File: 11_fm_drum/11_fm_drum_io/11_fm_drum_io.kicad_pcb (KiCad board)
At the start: 2 copper layers, 11 parts, among them J1 Conn_02x10_Counter_Clockwise, SW1 SW_SPDT, SW2 SW_SPDT

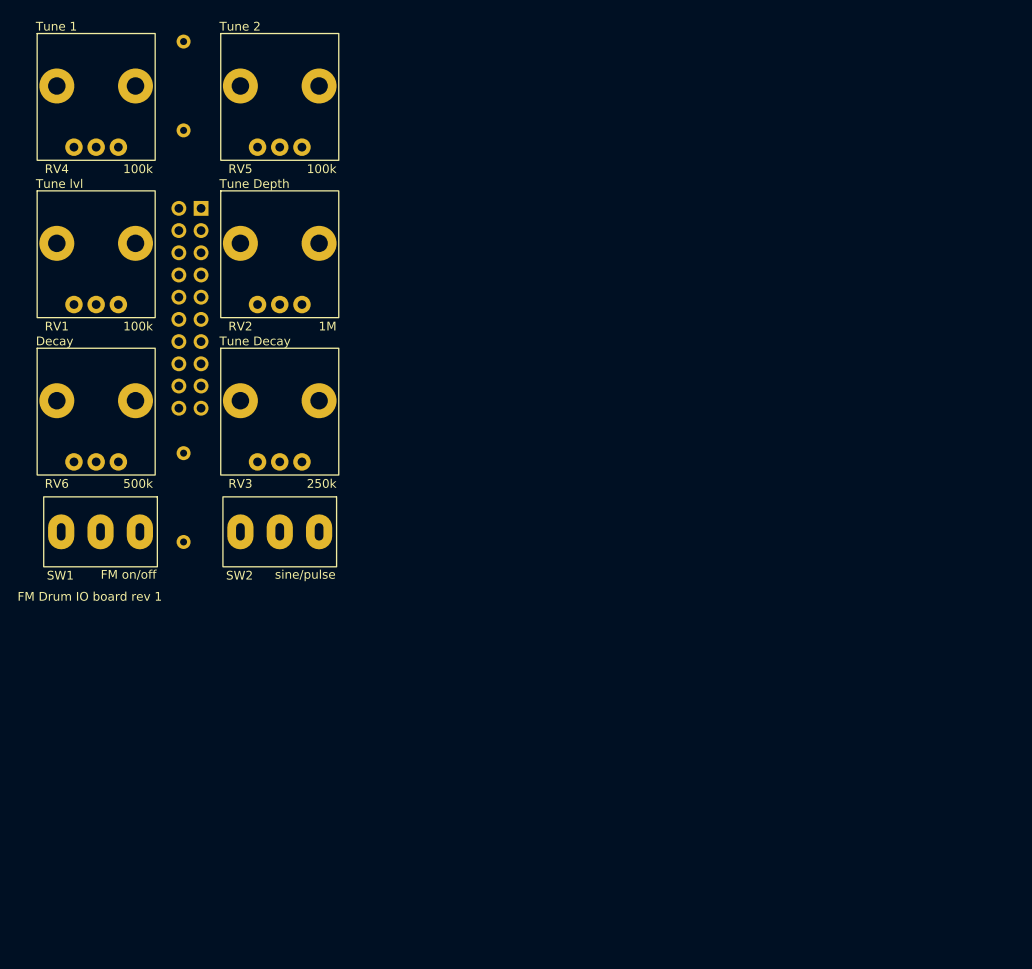
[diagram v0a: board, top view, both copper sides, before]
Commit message: removed io from 11
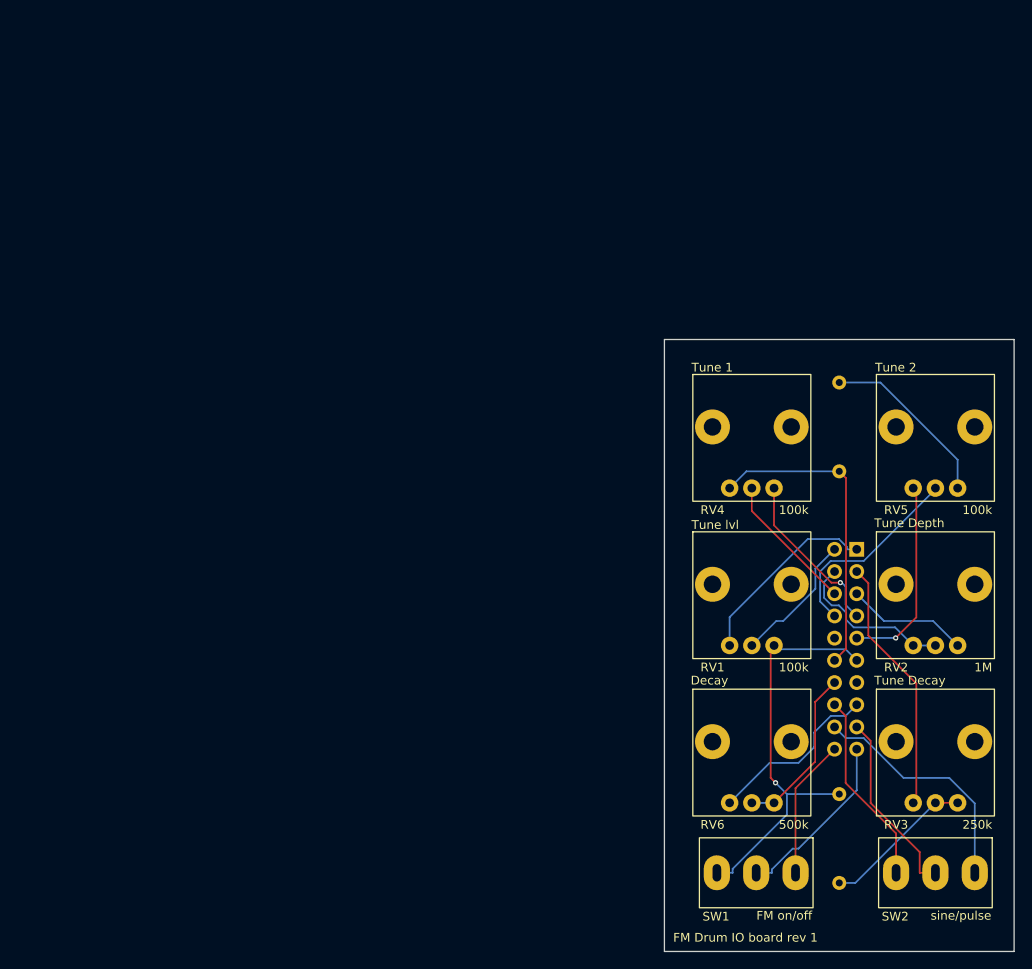
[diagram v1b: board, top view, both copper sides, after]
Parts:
- moved J1 84.5 mm to (97.0, 63.0)
- moved R1 84.5 mm to (95.0, 43.9)
- moved R2 84.5 mm to (95.0, 91.0)
- moved RV1 84.5 mm to (85.0, 67.0)
- moved RV2 84.5 mm to (106.0, 67.0)
- moved RV3 84.5 mm to (106.0, 85.0)
- moved RV4 84.5 mm to (85.0, 49.0)
- moved RV5 84.5 mm to (106.0, 49.0)
- moved RV6 84.5 mm to (85.0, 85.0)
- moved SW1 84.5 mm to (85.5, 100.0)
- moved SW2 84.5 mm to (106.0, 100.0)
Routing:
- net GND: track 0.00 -> 47.5 mm, vias 0 -> 1
- net +12V: track 0.00 -> 35.8 mm
- net io tune decay 1: track 0.00 -> 29.4 mm
- net io sine/pulse pin 1: track 0.00 -> 27.6 mm
- net io tune 2 pin 2: track 0.00 -> 23.0 mm
- net io tune 2 pin 3: track 0.00 -> 22.7 mm, vias 0 -> 1
- net io sine/pulse pin 3: track 0.00 -> 22.1 mm
- net io tune lvl pin 1: track 0.00 -> 22.1 mm
- net io sine/pulse pin 2: track 0.00 -> 21.5 mm
- net Net-(R1-Pad1): track 0.00 -> 20.4 mm
- net io fm on/off pin 2: track 0.00 -> 20.3 mm
- net io decay pin 1: track 0.00 -> 20.2 mm
- net io tune 1 pin 3: track 0.00 -> 19.2 mm, vias 0 -> 1
- net io decay pin 2: track 0.00 -> 19.2 mm
- net io tune depth 1: track 0.00 -> 19.0 mm
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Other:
- board outline added: 40 x 70 mm
